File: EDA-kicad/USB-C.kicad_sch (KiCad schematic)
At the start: 9 parts, among them J1 USBC-4-0-CX90MW9-24P1, U14 MUX HD3SS460RHRR, U15 USB SWITCH 2CHANNEL TS3USB221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

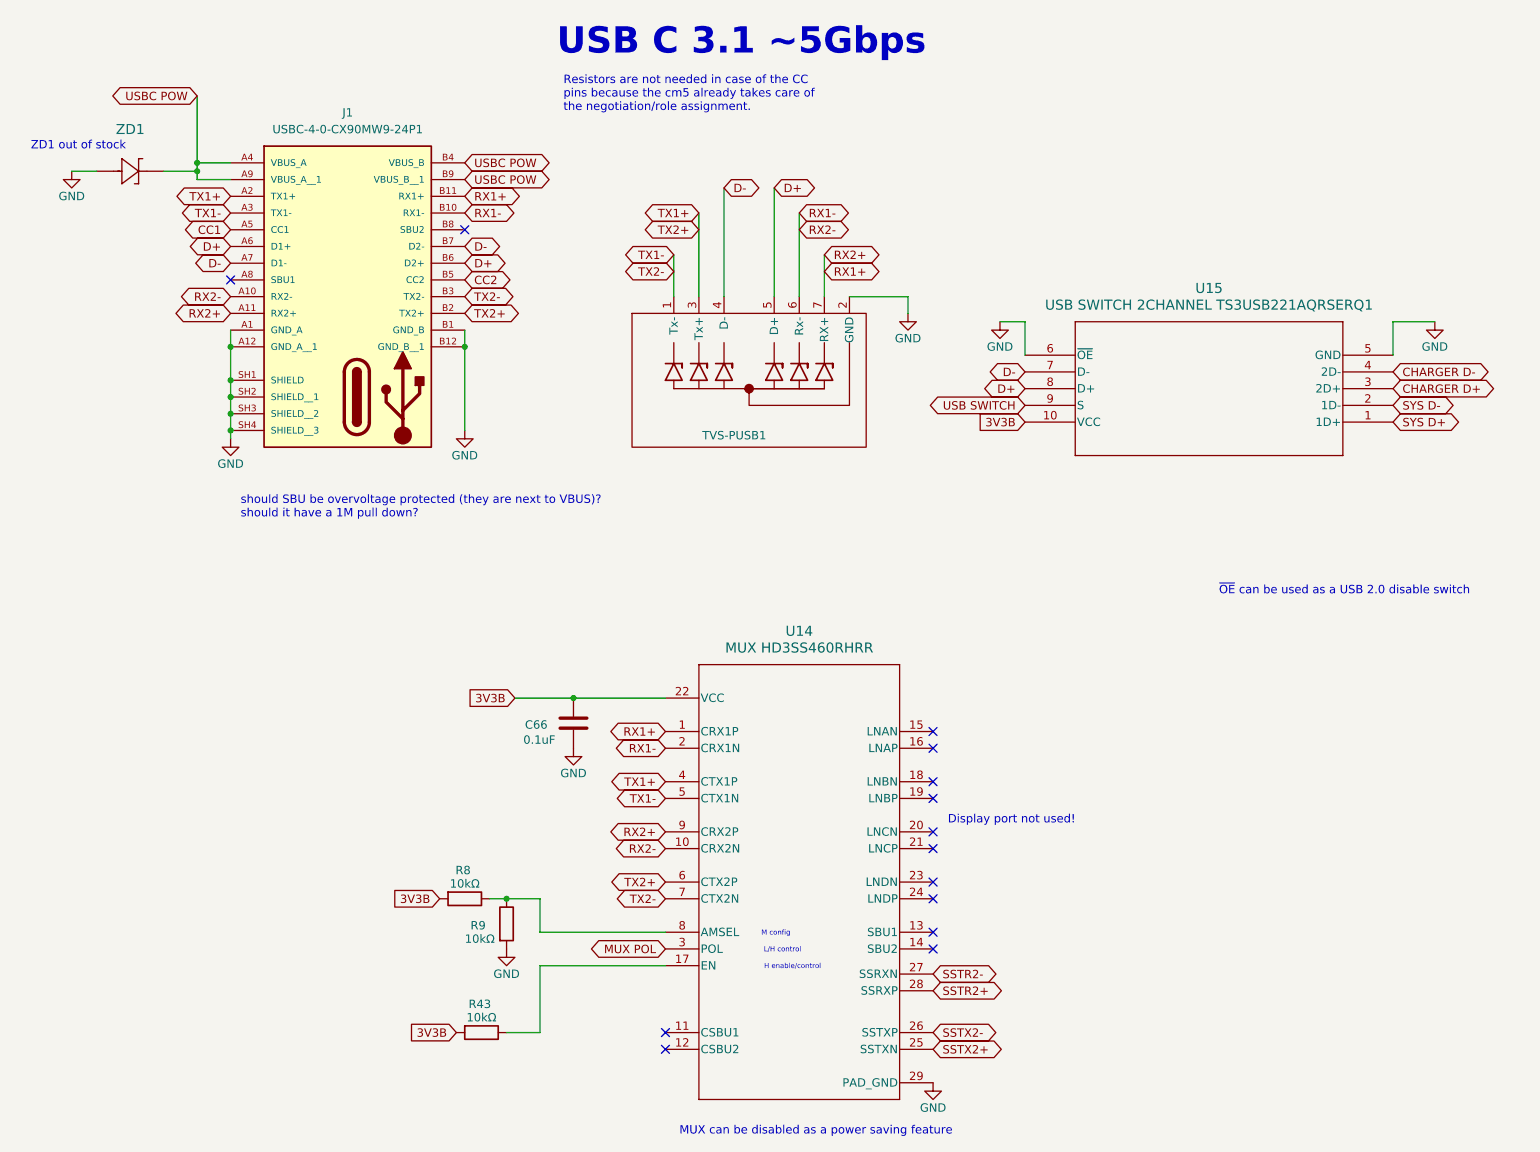
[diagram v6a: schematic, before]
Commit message: add image of selected MUX config
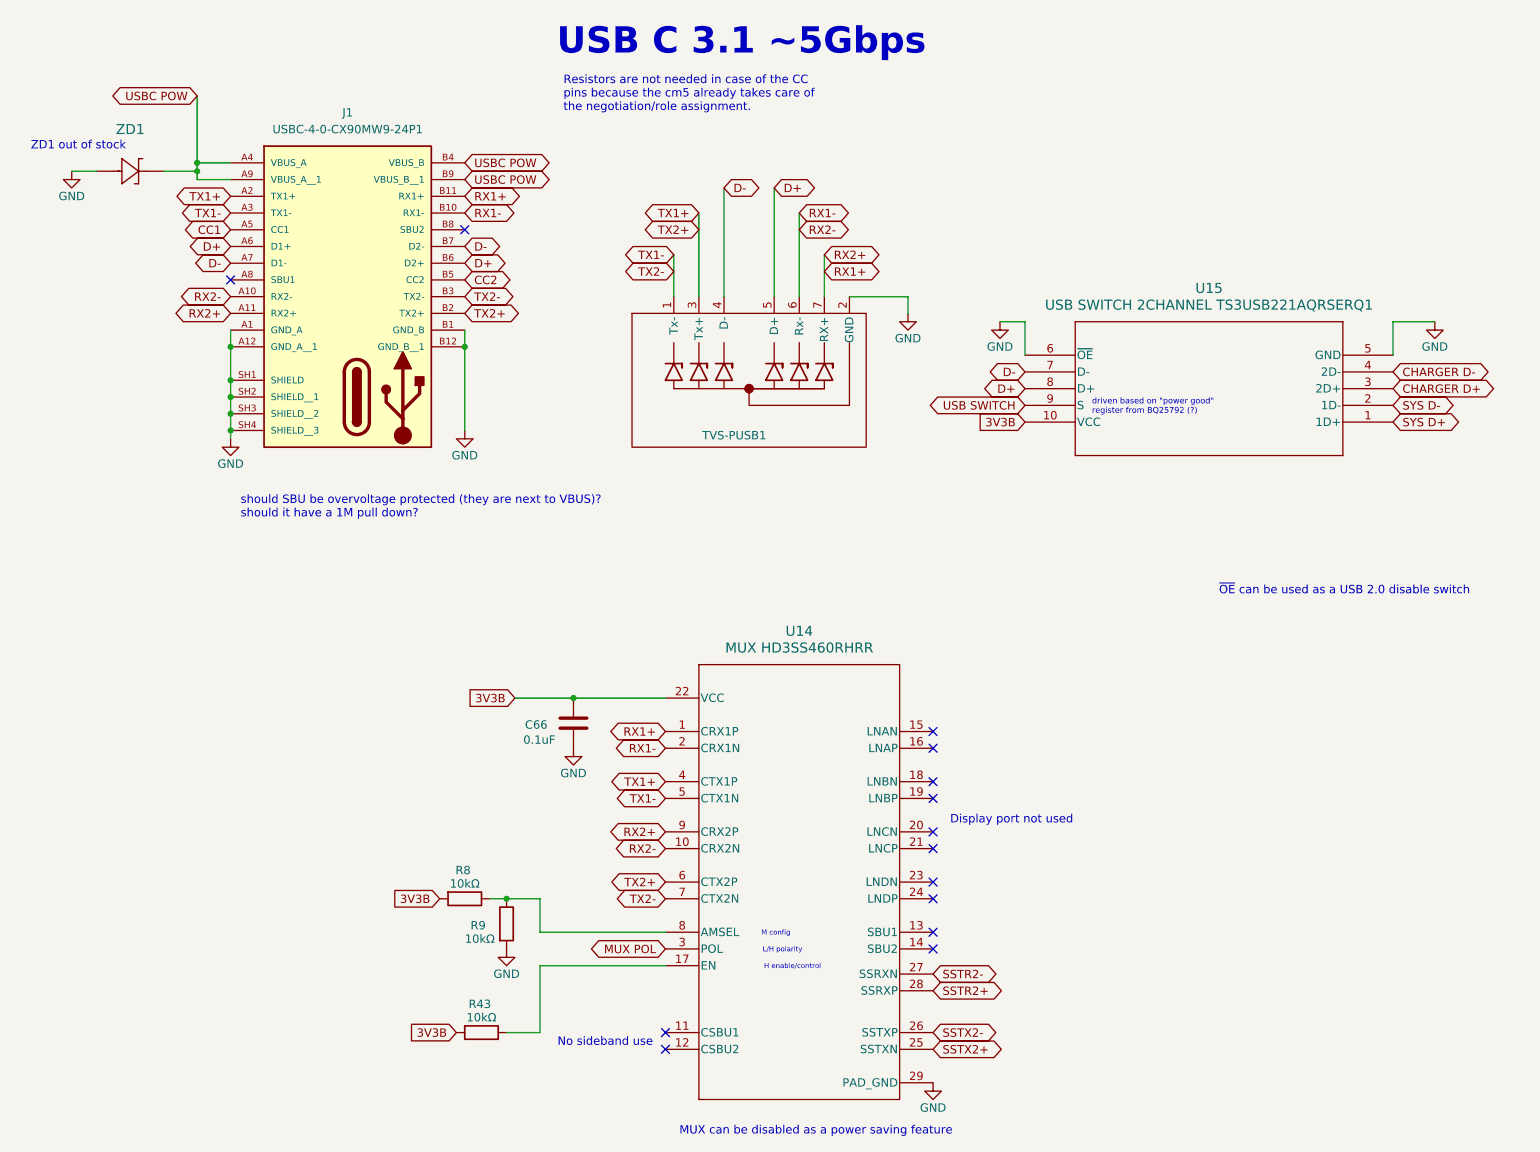
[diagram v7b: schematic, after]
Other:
- note added: "Display port not used"
- note added: "L/H polarity"
- note added: "No sideband use"
- note added: "driven based on "power good" register from BQ25792 (?)"
- note removed: "Display port not used!"
- note removed: "L/H control"
